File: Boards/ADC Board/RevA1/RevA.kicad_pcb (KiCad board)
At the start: 2 copper layers, 85 x 56 mm, 33 parts, among them J1 Left Connector, J10 Jumper Terminals, J11 Arduino Nano, J12 Arduino Nano, J13 Extra Pins, J14 Screw Terminals, J15 Screw Terminals, J16 Screw Terminals, J17 Screw Terminals, J2 Right Connector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

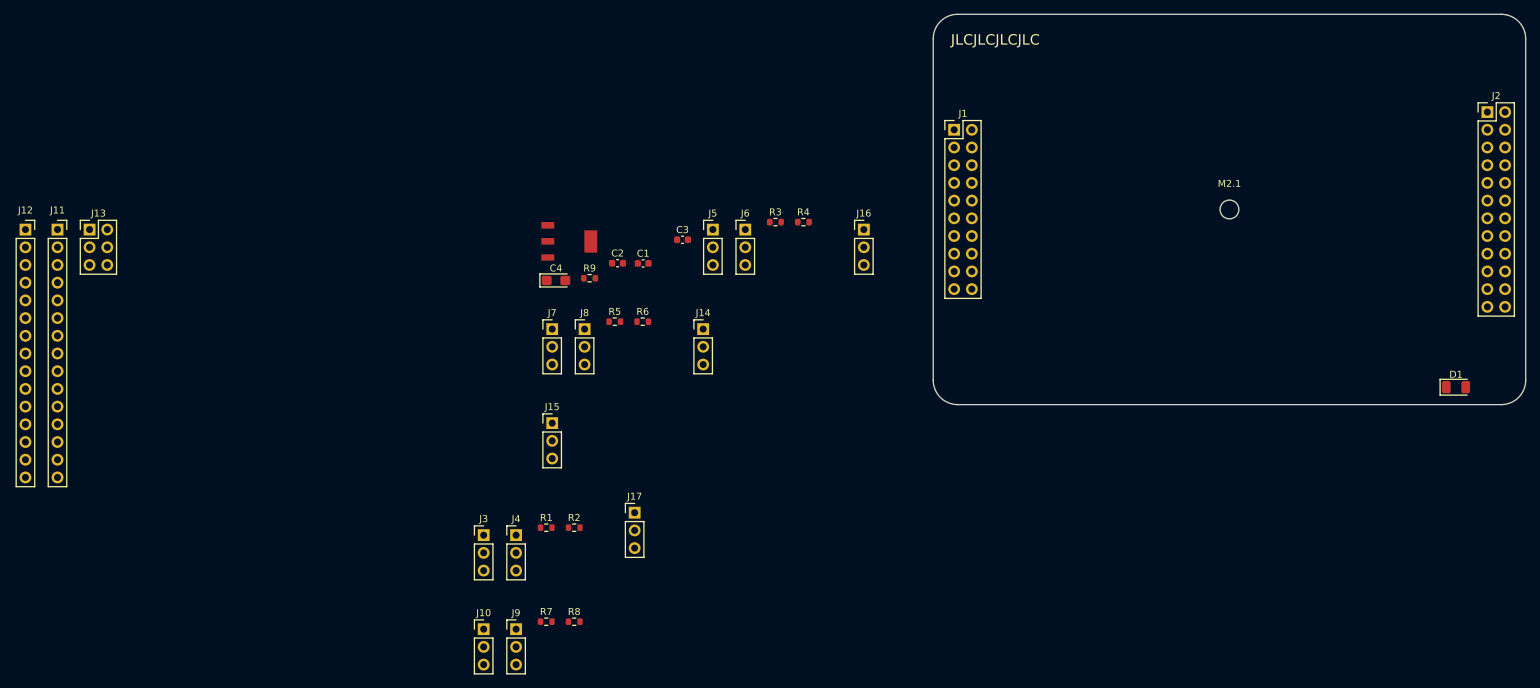
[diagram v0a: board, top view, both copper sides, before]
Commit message: Determined correct spacing for Arduino nano pins. Placed down voltage regulator and associated components.
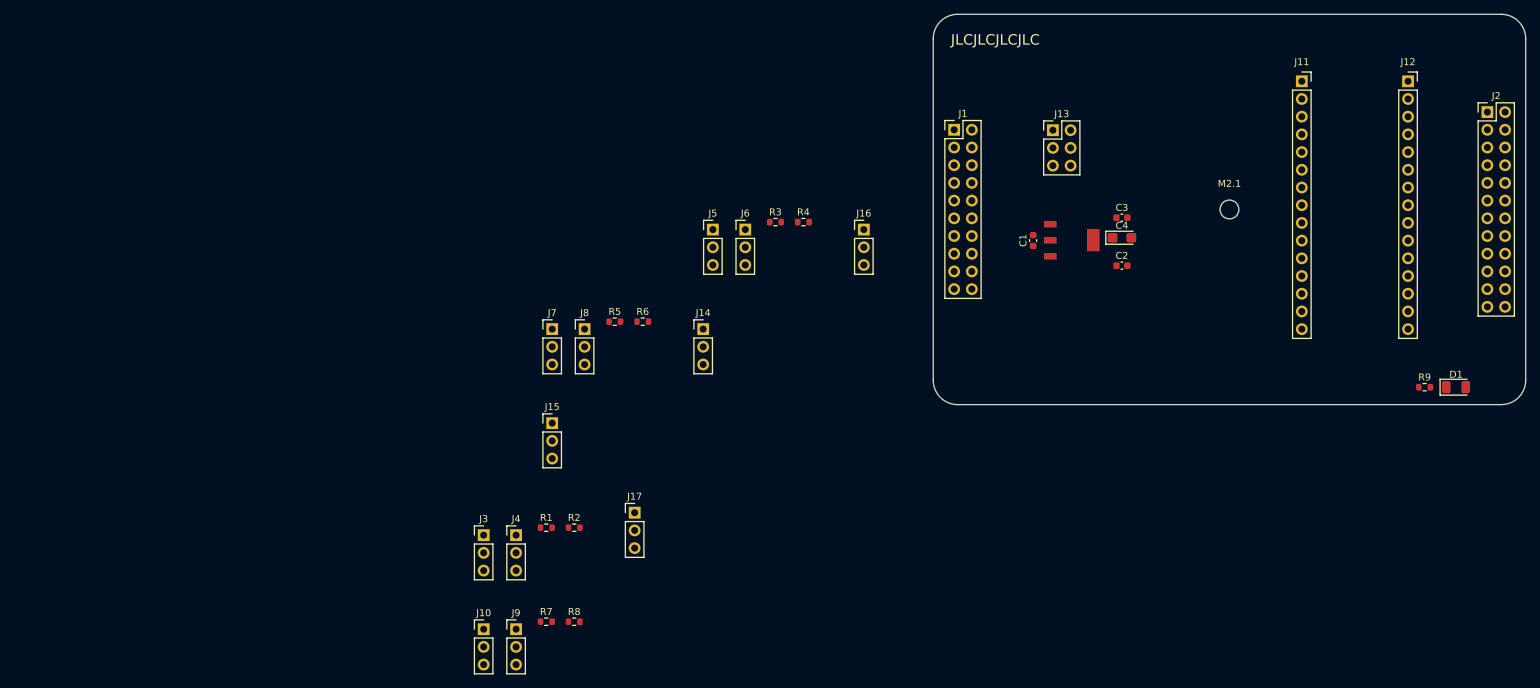
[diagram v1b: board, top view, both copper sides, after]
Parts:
- moved J12 199.5 mm to (228.1, 79.6)
- moved J11 179.8 mm to (212.9, 79.6)
- moved J13 138.9 mm to (177.2, 86.6)
- moved R9 120.8 mm to (230.5, 123.5)
- moved C4 81.4 mm to (187.1, 102.1)
- moved C2 72.4 mm to (187.1, 106.1)
- moved VR1 72.1 mm to (179.9, 102.4)
- moved C3 63.1 mm to (187.1, 99.2)
- moved C1 56.0 mm to (174.3, 102.5), turned to 90 degrees
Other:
- board text added: "SDAQ ADC Board Revision A Chris Walters (508) 975-3337 RIT BAJA"
- board text removed: "SDAQ ADC Board Revision A Chris Walters 508-975-3337 RIT BAJA"

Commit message: Added 12-pin and 4-pin spring terminal footprints. Updated footprints for ADC board. Continued work on PCB layout of ADC board.
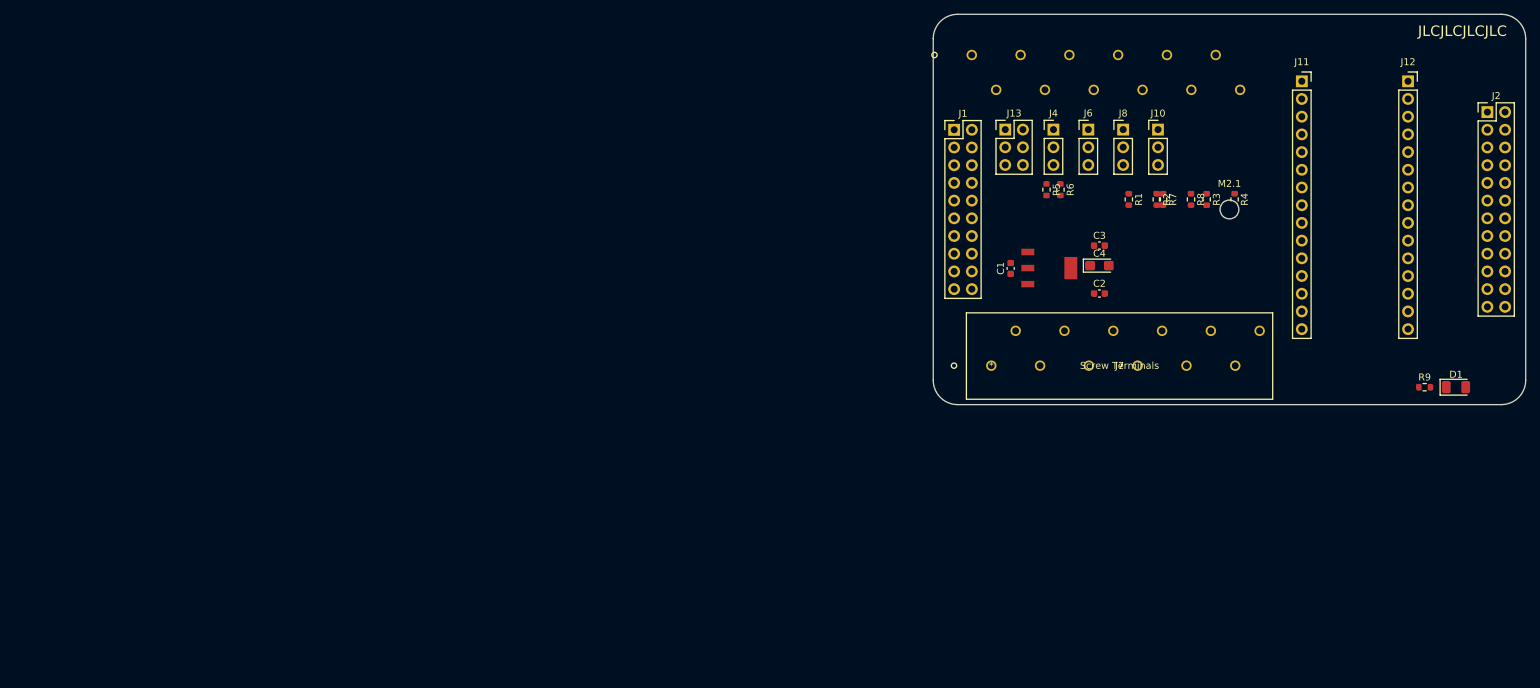
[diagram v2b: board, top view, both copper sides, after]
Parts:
- removed J14, J15, J17, J3, J5, J9: Screw Terminals, Connector_PinHeader_2.54mm:PinHeader_1x03_P2.54mm_Vertical
- J16: footprint Connector_PinHeader_2.54mm:PinHeader_1x03_P2.54mm_Vertical -> footprints:1985292; moved to B.Cu
- J7: footprint Connector_PinHeader_2.54mm:PinHeader_1x03_P2.54mm_Vertical -> footprints:1985292
- moved J10 120.4 mm to (192.2, 86.5)
- moved R8 107.2 mm to (197.0, 96.6), turned to 270 degrees
- moved R7 107.2 mm to (193.0, 96.6), turned to 270 degrees
- moved J4 96.6 mm to (177.2, 86.5)
- moved R1 95.9 mm to (188.1, 96.6), turned to 270 degrees
- moved R2 95.9 mm to (192.1, 96.6), turned to 270 degrees
- moved J8 82.4 mm to (187.2, 86.5)
- moved R5 64.8 mm to (176.2, 95.2), turned to 270 degrees
- moved J7 63.2 mm to (168.3, 120.4)
- moved R6 62.8 mm to (178.2, 95.2), turned to 270 degrees
- moved R4 61.9 mm to (203.2, 96.6), turned to 270 degrees
- moved R3 61.9 mm to (199.2, 96.6), turned to 270 degrees
- moved J6 51.3 mm to (182.2, 86.5)
- moved J16 29.4 mm to (165.5, 75.8)
- moved J13 6.84 mm to (170.3, 86.5)
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
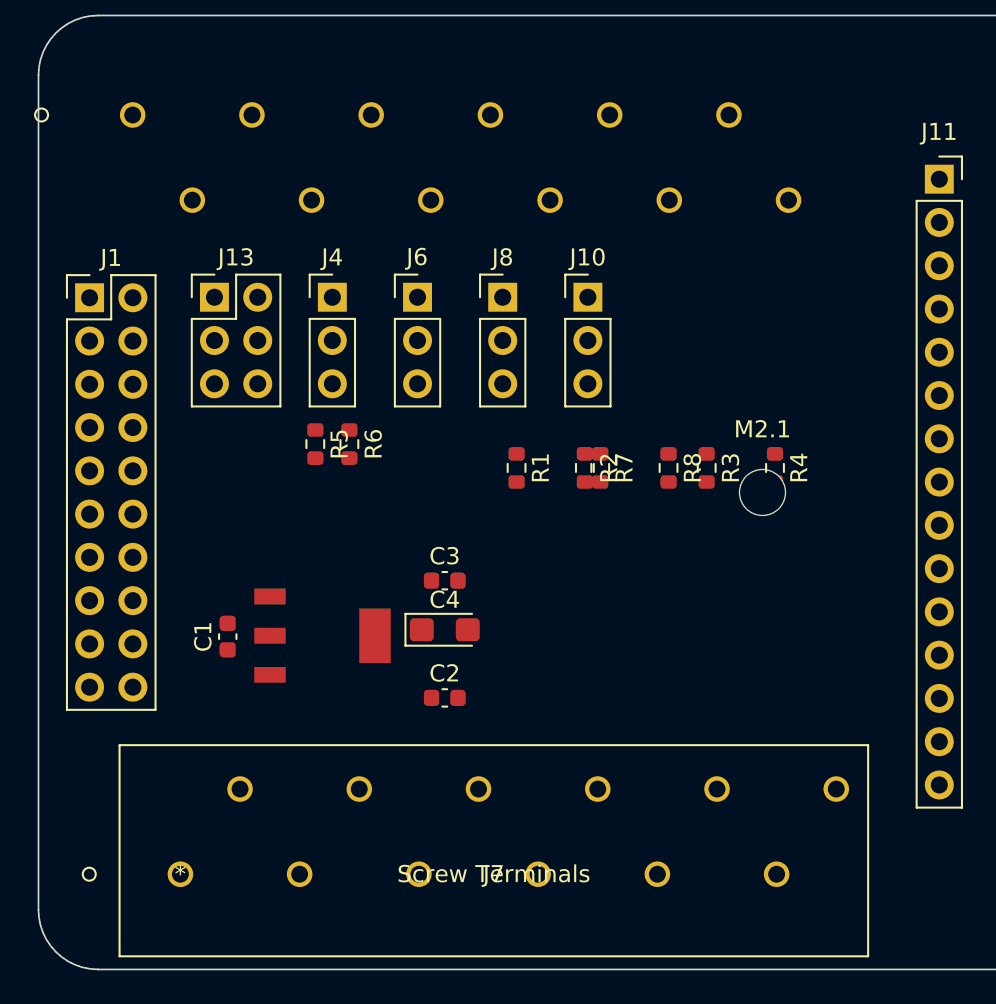
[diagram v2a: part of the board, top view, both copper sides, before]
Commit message: Imported 4 pin spring terminals. Replaced 12 pin terminals with 4 pin terminals on ADC board. Placed 4 pin terminals on PCB.
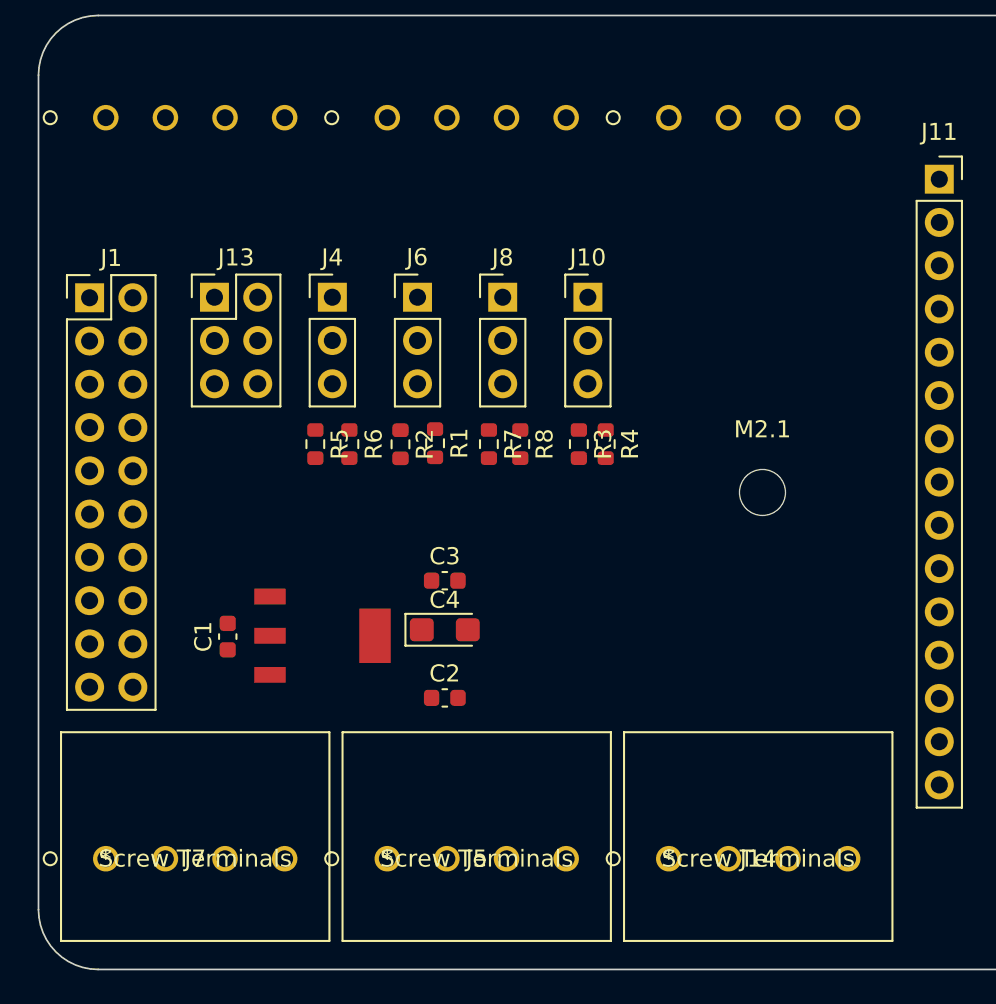
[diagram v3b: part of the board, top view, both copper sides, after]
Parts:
- added J14: Screw Terminals, Spring_Terminal_4Pin:1984989, F.Cu at (197.0, 119.5)
- added J3: Screw Terminals, Spring_Terminal_4Pin:1984989, B.Cu at (180.5, 76.0)
- added J5: Screw Terminals, Spring_Terminal_4Pin:1984989, F.Cu at (180.5, 119.5)
- added J9: Screw Terminals, Spring_Terminal_4Pin:1984989, B.Cu at (197.0, 76.0)
- J16, J7: footprint footprints:1985292 -> Spring_Terminal_4Pin:1984989
- moved R2 10.9 mm to (181.2, 95.2)
- moved R4 10.0 mm to (193.3, 95.2)
- moved R8 8.82 mm to (188.3, 95.2)
- moved R3 7.63 mm to (191.7, 95.2)
- moved R7 6.68 mm to (186.4, 95.2)
- moved R1 5.00 mm to (183.3, 95.1)
- moved J7 4.47 mm to (163.9, 119.5)
- moved J16 1.59 mm to (163.9, 76.0)
